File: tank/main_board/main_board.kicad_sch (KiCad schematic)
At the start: 44 parts, among them J1 Encoder0, J10 Spk, J11 LEDs, J12 SigOut, J13 M2, J14 M1, J15 M0, J2 Encoder1, J3 Encoder2, J4 Encoder3, J5 Bump0, J6 Bump1, J7 Programming Header, J8 PowerOut, J9 PowerIn, U1 L7805, U2 ATMEGA328P-PU, U3 SN74HC595, U4 L293D, U5 L293D, Y1 Crystal

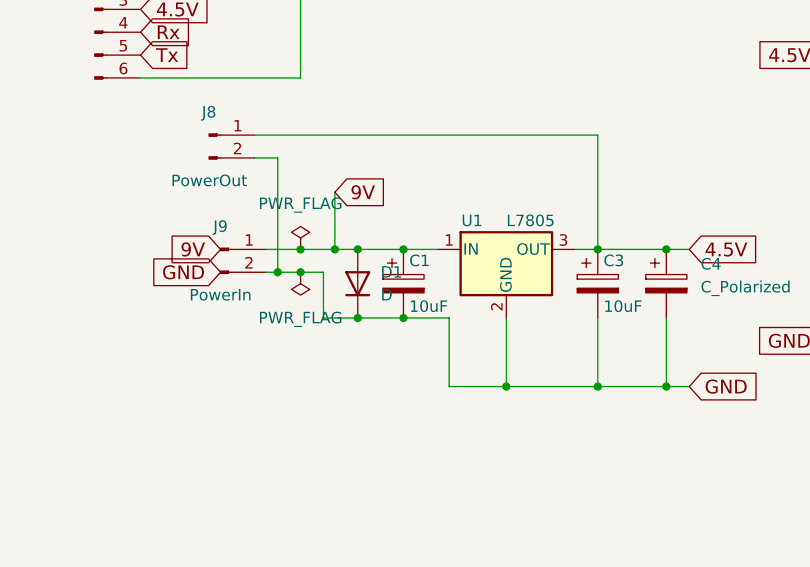
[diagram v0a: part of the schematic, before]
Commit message: LED Strip v0.5 - Change LED strip from 3 LEDs to 4
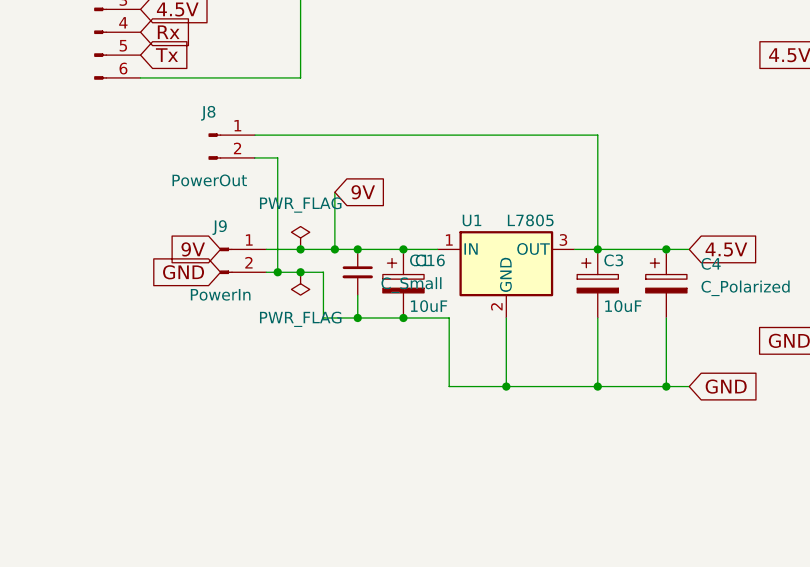
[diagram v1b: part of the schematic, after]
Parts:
- removed D1: D, Diode_THT:D_DO-15_P10.16mm_Horizontal, symbol Device:D
- added C16: C_Small, Capacitor_THT:C_Disc_D5.0mm_W2.5mm_P2.50mm, symbol Device:C_Small
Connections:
- net 9V: now also C16.1
- net GND: now also C16.2
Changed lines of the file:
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@@
 	)
 	(junction
-		(at 48.26 130.81)
-		(diameter 0)
-		(color 0 0 0 0)
-	)
-	(junction
 		(at 41.91 125.73)
 		(diameter 0)
@@
 	)
 	(junction
+		(at 48.26 130.81)
+		(diameter 0)
+		(color 0 0 0 0)
+	)
+	(junction
 		(at 196.85 95.25)
 		(diameter 0)
@@
 	)
 	(junction
+		(at 48.26 123.19)
+		(diameter 0)
+		(color 0 0 0 0)
+	)
+	(junction
 		(at 187.96 161.29)
 		(diameter 0)
@@
 	)
 	(junction
-		(at 48.26 123.19)
-		(diameter 0)
-		(color 0 0 0 0)
-	)
-	(junction
 		(at 191.77 95.25)
 		(diameter 0)
@@
 	(wire
 		(pts
+			(xy 48.26 128.27) (xy 48.26 130.81)
+		)
+		(stroke
+			(width 0)
+			(type default)
+		)
+	)
+	(wire
+		(pts
+			(xy 48.26 130.81) (xy 53.34 130.81)
+		)
+		(stroke
+			(width 0)
+			(type default)
+		)
+	)
+	(wire
+		(pts
 			(xy 210.82 64.77) (xy 218.44 64.77)
 		)
@@
 	(wire
 		(pts
+			(xy 48.26 123.19) (xy 53.34 123.19)
+		)
+		(stroke
+			(width 0)
+			(type default)
+		)
+	)
+	(wire
+		(pts
 			(xy 74.93 110.49) (xy 74.93 123.19)
 		)
@@
 	(wire
 		(pts
-			(xy 45.72 123.19) (xy 48.26 123.19)
-		)
-		(stroke
-			(width 0)
-			(type default)
-		)
-	)
-	(wire
-		(pts
 			(xy 210.82 77.47) (xy 222.25 77.47)
 		)
@@
 	(wire
 		(pts
-			(xy 48.26 123.19) (xy 53.34 123.19)
+			(xy 45.72 123.19) (xy 48.26 123.19)
 		)
 		(stroke
@@
 	(wire
 		(pts
-			(xy 48.26 130.81) (xy 53.34 130.81)
-		)
-		(stroke
-			(width 0)
-			(type default)
-		)
-	)
-	(wire
-		(pts
 			(xy 140.97 67.31) (xy 143.51 67.31)
 		)
@@
 	)
 	(symbol
-		(lib_id "Device:D")
-		(at 48.26 127 90)
+		(lib_id "Connector:Conn_01x03_Pin")
+		(at 19.05 48.26 0)
 		(unit 1)
 		(exclude_from_sim no)
@@
 		(on_board yes)
 		(dnp no)
-		(fields_autoplaced yes)
-		(property "Reference" "D1"
-			(at 50.8 125.7299 90)
+		(property "Reference" "J3"
+			(at 19.05 43.18 0)
 			(effects
 				(font
 					(size 1.27 1.27)
 				)
-				(justify right)
 			)
 		)
-		(property "Value" "D"
-			(at 50.8 128.2699 90)
+		(property "Value" "Encoder2"
+			(at 19.05 43.18 0)
 			(effects
 				(font
 					(size 1.27 1.27)
 				)
-				(justify right)
 			)
 		)
-		(property "Footprint" "Diode_THT:D_DO-15_P10.16mm_Horizontal"
-			(at 48.26 127 0)
+		(property "Footprint" "Connector_JST:JST_EH_B3B-EH-A_1x03_P2.50mm_Vertical"
+			(at 19.05 48.26 0)
 			(effects
 				(font
@@
 		)
 		(property "Datasheet" "~"
-			(at 48.26 127 0)
-			(effects
-				(font
-					(size 1.27 1.27)
-				)
-				(hide yes)
-			)
-		)
-		(property "Description" "Diode"
-			(at 48.26 127 0)
-			(effects
-				(font
-					(size 1.27 1.27)
-				)
-				(hide yes)
-			)
-		)
-		(property "Sim.Device" "D"
-			(at 48.26 127 0)
+			(at 19.05 48.26 0)
 			(effects
 				(font
@@
 			)
 		)
-		(property "Sim.Pins" "1=K 2=A"
-			(at 48.26 127 0)
+		(property "Description" "Generic connector, single row, 01x03, script generated"
+			(at 19.05 48.26 0)
 			(effects
 				(font
@@
 		(pin "2"
 		)
+		(pin "3"
+		)
 		(instances
 			(project ""
 				(path "/5e61a6ca-2010-47b5-82c1-56d3dc23b23a"
-					(reference "D1")
+					(reference "J3")
 					(unit 1)
 				)
@@
 	)
 	(symbol
-		(lib_id "Connector:Conn_01x03_Pin")
-		(at 19.05 48.26 0)
+		(lib_id "Device:C_Small")
+		(at 143.51 69.85 0)
 		(unit 1)
 		(exclude_from_sim no)
@@
 		(on_board yes)
 		(dnp no)
-		(property "Reference" "J3"
-			(at 19.05 43.18 0)
+		(property "Reference" "C6"
+			(at 145.8468 68.6816 0)
 			(effects
 				(font
 					(size 1.27 1.27)
 				)
+				(justify left)
 			)
 		)
-		(property "Value" "Encoder2"
-			(at 19.05 43.18 0)
+		(property "Value" "100nF"
+			(at 145.8468 70.993 0)
 			(effects
 				(font
 					(size 1.27 1.27)
 				)
+				(justify left)
 			)
 		)
-		(property "Footprint" "Connector_JST:JST_EH_B3B-EH-A_1x03_P2.50mm_Vertical"
-			(at 19.05 48.26 0)
+		(property "Footprint" "Capacitor_THT:C_Disc_D5.0mm_W2.5mm_P2.50mm"
+			(at 143.51 69.85 0)
 			(effects
 				(font
@@
 		)
 		(property "Datasheet" "~"
-			(at 19.05 48.26 0)
+			(at 143.51 69.85 0)
 			(effects
 				(font
@@
 			)
 		)
-		(property "Description" "Generic connector, single row, 01x03, script generated"
-			(at 19.05 48.26 0)
+		(property "Description" "Unpolarized capacitor, small symbol"
+			(at 143.51 69.85 0)
 			(effects
 				(font
@@
 		(pin "2"
 		)
-		(pin "3"
-		)
 		(instances
 			(project ""
 				(path "/5e61a6ca-2010-47b5-82c1-56d3dc23b23a"
-					(reference "J3")
+					(reference "C6")
 					(unit 1)
 				)
@@
 	(symbol
 		(lib_id "Device:C_Small")
-		(at 143.51 69.85 0)
+		(at 222.25 118.11 180)
 		(unit 1)
 		(exclude_from_sim no)
@@
 		(on_board yes)
 		(dnp no)
-		(property "Reference" "C6"
-			(at 145.8468 68.6816 0)
+		(property "Reference" "C15"
+			(at 221.996 119.888 0)
 			(effects
 				(font
@@
 			)
 		)
-		(property "Value" "100nF"
-			(at 145.8468 70.993 0)
+		(property "Value" ".1uF"
+			(at 221.996 116.078 0)
 			(effects
 				(font
@@
 		)
 		(property "Footprint" "Capacitor_THT:C_Disc_D5.0mm_W2.5mm_P2.50mm"
-			(at 143.51 69.85 0)
+			(at 222.25 118.11 0)
 			(effects
 				(font
@@
 		)
 		(property "Datasheet" "~"
-			(at 143.51 69.85 0)
+			(at 222.25 118.11 0)
 			(effects
 				(font
@@
 		)
 		(property "Description" "Unpolarized capacitor, small symbol"
-			(at 143.51 69.85 0)
+			(at 222.25 118.11 0)
 			(effects
 				(font
@@
 		)
 		(instances
-			(project ""
+			(project "main_board"
 				(path "/5e61a6ca-2010-47b5-82c1-56d3dc23b23a"
-					(reference "C6")
+					(reference "C15")
 					(unit 1)
 				)
@@
 	(symbol
 		(lib_id "Device:C_Small")
-		(at 222.25 118.11 180)
+		(at 48.26 125.73 0)
 		(unit 1)
 		(exclude_from_sim no)
@@
 		(on_board yes)
 		(dnp no)
-		(property "Reference" "C15"
-			(at 221.996 119.888 0)
+		(property "Reference" "C16"
+			(at 54.61 124.46 0)
 			(effects
 				(font
@@
 			)
 		)
-		(property "Value" ".1uF"
-			(at 221.996 116.078 0)
+		(property "Value" "C_Small"
+			(at 50.8 127.0062 0)
 			(effects
 				(font
@@
 		)
 		(property "Footprint" "Capacitor_THT:C_Disc_D5.0mm_W2.5mm_P2.50mm"
-			(at 222.25 118.11 0)
+			(at 48.26 125.73 0)
 			(effects
 				(font
@@
 		)
 		(property "Datasheet" "~"
-			(at 222.25 118.11 0)
+			(at 48.26 125.73 0)
 			(effects
 				(font
@@
 		)
 		(property "Description" "Unpolarized capacitor, small symbol"
-			(at 222.25 118.11 0)
+			(at 48.26 125.73 0)
 			(effects
 				(font
@@
 			(project "main_board"
 				(path "/5e61a6ca-2010-47b5-82c1-56d3dc23b23a"
-					(reference "C15")
+					(reference "C16")
 					(unit 1)
 				)

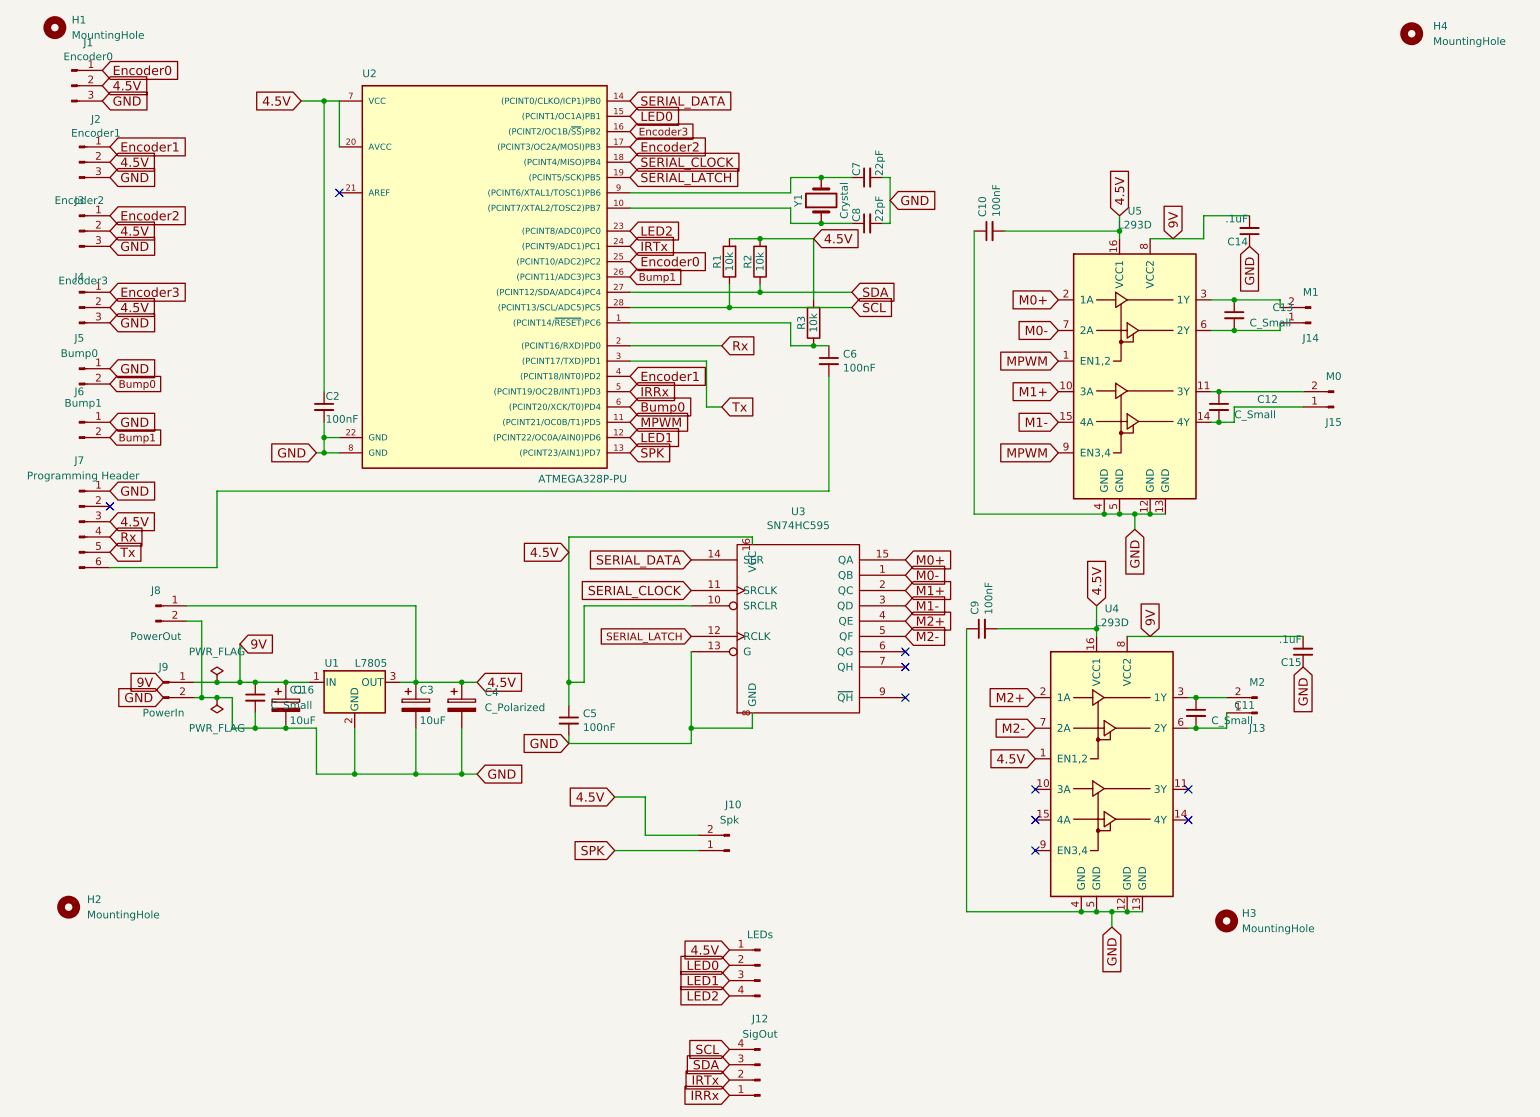
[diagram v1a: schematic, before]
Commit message: Main Board v0.20
0.19 was a bust, motor-wise. So I made motor traces 1.2mm wide.

Now LED connector is 4-pins, for always-on LED.

Added capacitors to bump switches.
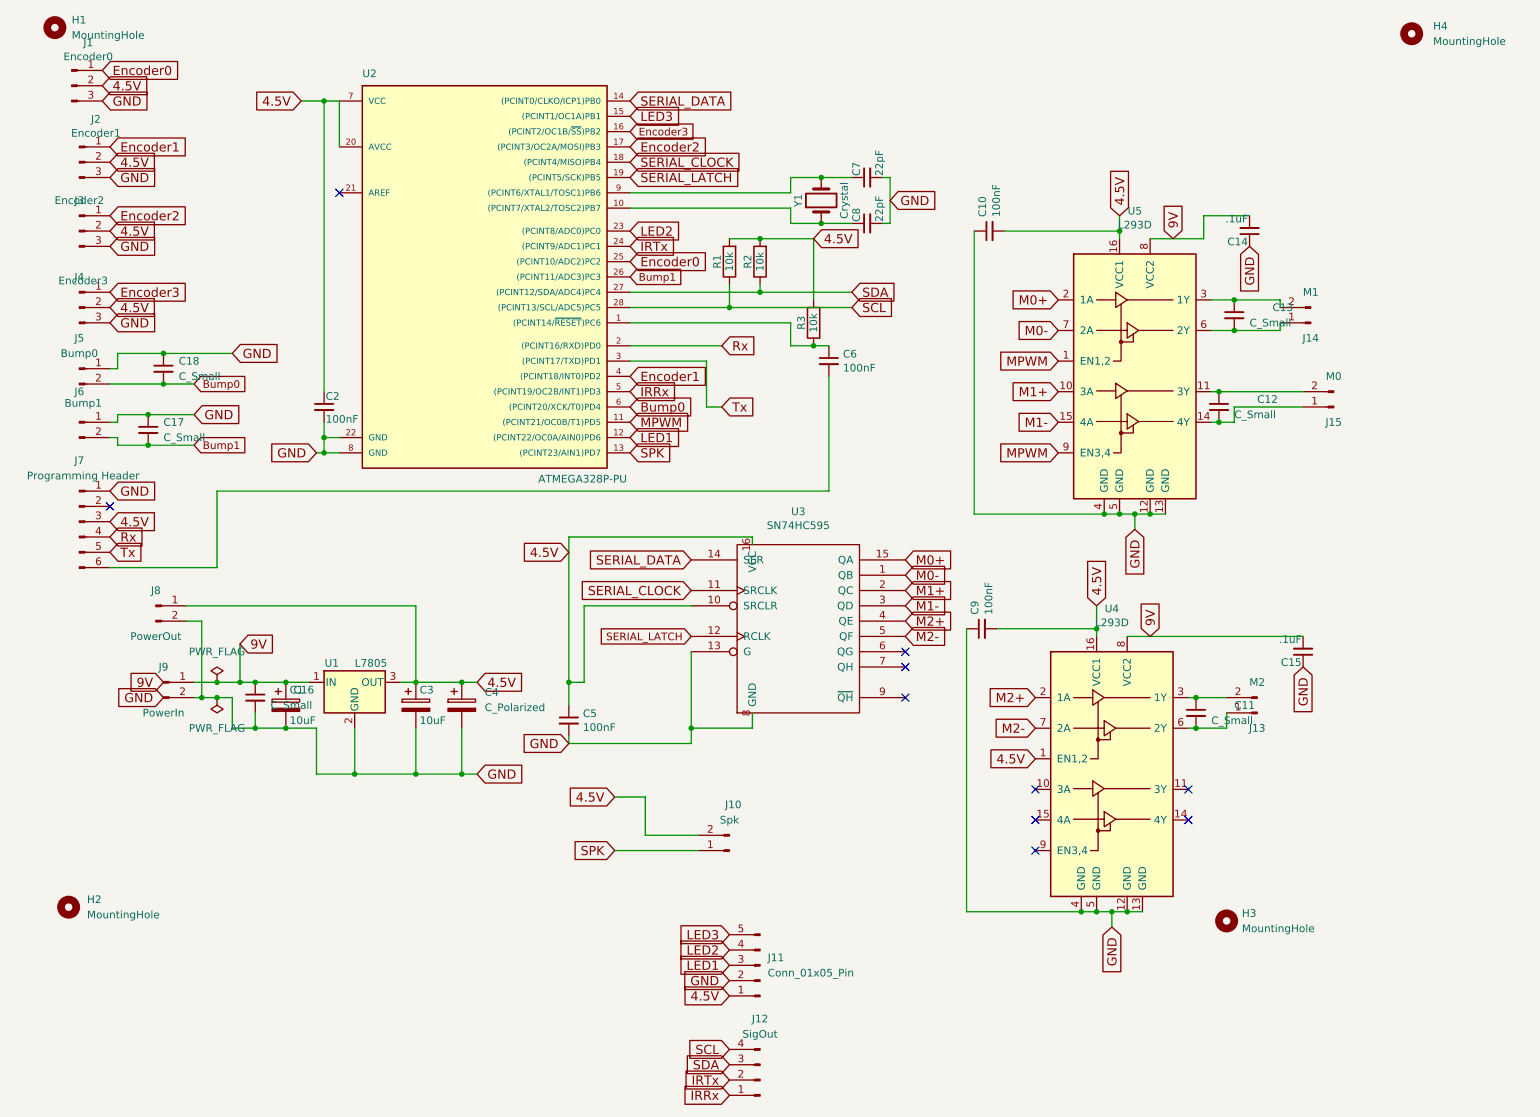
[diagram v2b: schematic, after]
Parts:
- removed J11: LEDs, Connector_JST:JST_EH_B4B-EH-A_1x04_P2.50mm_Vertical, symbol Connector:Conn_01x04_Pin
- added C17, C18: C_Small, Capacitor_THT:C_Disc_D5.0mm_W2.5mm_P2.50mm, symbol Device:C_Small
- added J11: Conn_01x05_Pin, Connector_JST:JST_EH_B5B-EH-A_1x05_P2.50mm_Vertical, symbol Connector:Conn_01x05_Pin
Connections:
- net 4.5V: now also J11.1 (Pin_1)
- net Bump0: now also C18.2
- net Bump1: now also C17.2
- net GND: now also C17.1, C18.1, J11.2 (Pin_2)
- net LED1: now also J11.3 (Pin_3)
- net LED2: now also J11.4 (Pin_4)
- net LED0 renamed LED3
- net LED3: now also J11.5 (Pin_5)
